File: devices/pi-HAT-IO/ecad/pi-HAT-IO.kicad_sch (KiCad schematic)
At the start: 49 parts, among them J1 GPIO, J10 JST XH, J2 Mini-Fit Jr, J3 JST SH, J4 JST SH, J5 JST SH, J6 PC FAN HEADER, J7 PC FAN HEADER, J8 JST PH, J9 JST PH, Q1 SI4477DY-T1-GE3, Q2 DMMT5401-7-F, Q3 DMG2305UX, Q4 DMG2305UX, U1 TLV75733PDBV, U2 PMU8418, U3 TCA9406DCTR, U4 EMC2302, U5 MCP9804_DFN

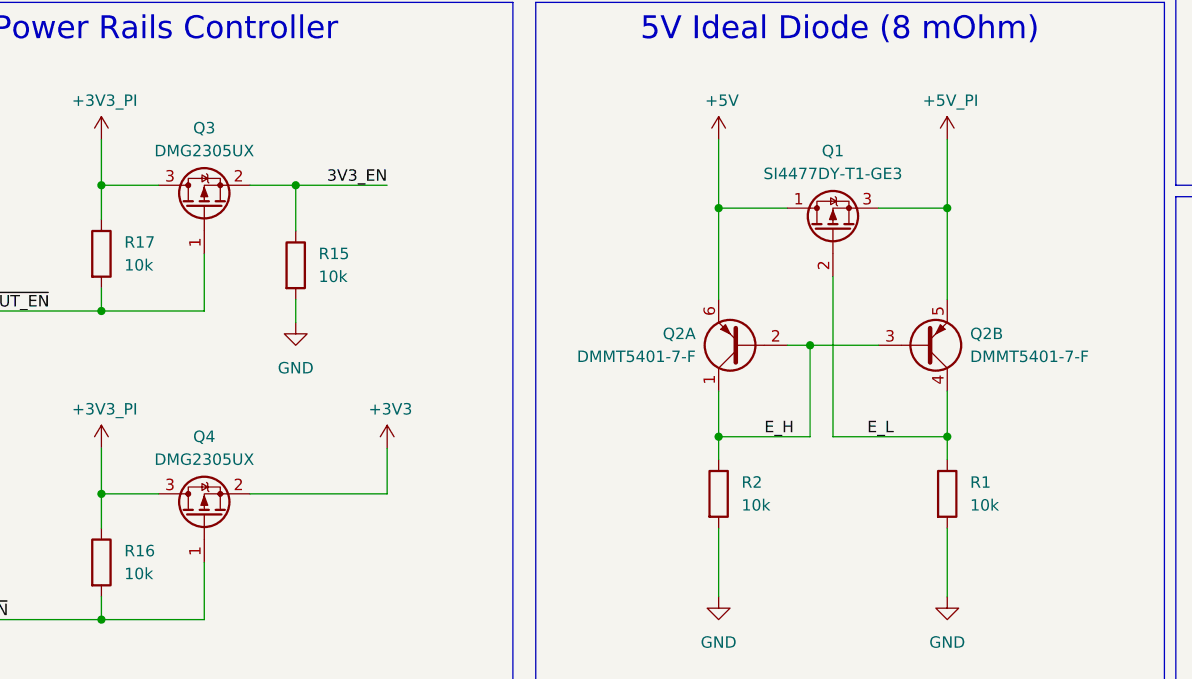
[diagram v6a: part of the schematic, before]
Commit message: Corrects PCB for production'
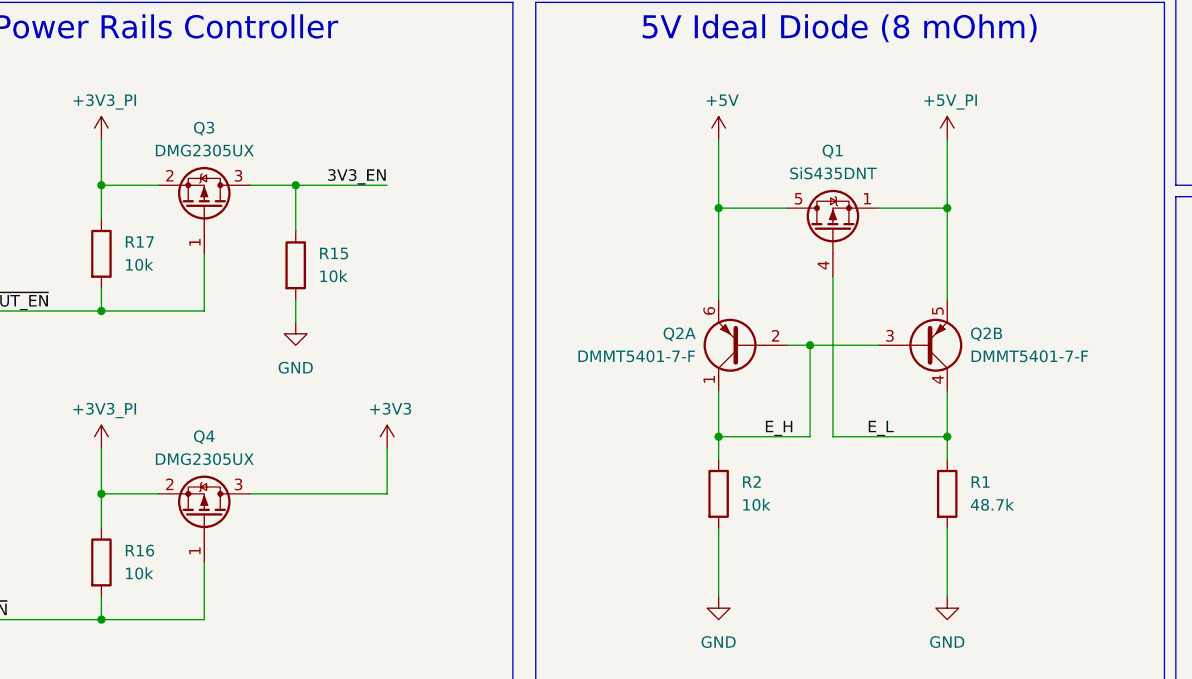
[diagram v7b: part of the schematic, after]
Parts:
- removed Q1: SI4477DY-T1-GE3, Package_SO:SO-8_3.9x4.9mm_P1.27mm, symbol Device:Q_PMOS_DGS
- added Q1: SiS435DNT, Package_SO:Vishay_PowerPAK_1212-8_Single, symbol Transistor_FET:SiS415DNT
- R1: value 10k -> 48.7k
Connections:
- net +3V3: now also Q4.3 (D); no longer Q4.2 (S)
- net +3V3_PI: now also Q3.2 (S), Q4.2 (S); no longer Q3.3 (D), Q4.3 (D)
- net +5V: now also Q1.5 (D)
- net +5V_PI: now also Q1.1 (S), Q1.2 (S), Q1.3 (S)
- net 3V3_EN: now also Q3.3 (D); no longer Q3.2 (S)
- net E_L: now also Q1.4 (G)
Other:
- moved on the sheet: Q3, Q4
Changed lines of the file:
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@@
 			)
 		)
-		(property "Value" "10k"
+		(property "Value" "48.7k"
 			(at 288.29 128.2699 0)
 			(effects
@@
 	)
 	(symbol
-		(lib_id "Device:Q_PMOS_DGS")
-		(at 273.05 97.79 90)
-		(unit 1)
-		(exclude_from_sim no)
-		(in_bom yes)
-		(on_board yes)
-		(dnp no)
-		(fields_autoplaced yes)
-		(property "Reference" "Q1"
-			(at 273.05 88.9 90)
-			(effects
-				(font
-					(size 1.27 1.27)
-				)
-			)
-		)
-		(property "Value" "SI4477DY-T1-GE3"
-			(at 273.05 91.44 90)
-			(effects
-				(font
-					(size 1.27 1.27)
-				)
-			)
-		)
-		(property "Footprint" "Package_SO:SO-8_3.9x4.9mm_P1.27mm"
-			(at 270.51 92.71 0)
-			(effects
-				(font
-					(size 1.27 1.27)
-				)
-				(hide yes)
-			)
-		)
-		(property "Datasheet" "~"
-			(at 273.05 97.79 0)
-			(effects
-				(font
-					(size 1.27 1.27)
-				)
-				(hide yes)
-			)
-		)
-		(property "Description" "P-MOSFET transistor, drain/gate/source"
-			(at 273.05 97.79 0)
-			(effects
-				(font
-					(size 1.27 1.27)
-				)
-				(hide yes)
-			)
-		)
-		(property "MPN" "SI4477DY-T1-GE3"
-			(at 273.05 97.79 90)
-			(effects
-				(font
-					(size 1.27 1.27)
-				)
-				(hide yes)
-			)
-		)
-		(property "Power Rating" ""
-			(at 273.05 97.79 0)
-			(effects
-				(font
-					(size 1.27 1.27)
-				)
-				(hide yes)
-			)
-		)
-		(property "Tolerance" ""
-			(at 273.05 97.79 0)
-			(effects
-				(font
-					(size 1.27 1.27)
-				)
-				(hide yes)
-			)
-		)
-		(property "Manufacturer" "Vishay Siliconix"
-			(at 273.05 97.79 0)
-			(effects
-				(font
-					(size 1.27 1.27)
-				)
-				(hide yes)
-			)
-		)
-		(pin "2"
-		)
-		(pin "3"
-		)
-		(pin "1"
-		)
-		(instances
-			(project "pi-HAT-IO"
-				(path "/e63e39d7-6ac0-4ffd-8aa3-1841a4541b55"
-					(reference "Q1")
-					(unit 1)
-				)
-			)
-		)
-	)
-	(symbol
 		(lib_id "power:+5V")
 		(at 346.71 26.67 0)
@@
 	)
 	(symbol
+		(lib_id "Transistor_FET:SiS415DNT")
+		(at 273.05 97.79 90)
+		(unit 1)
+		(exclude_from_sim no)
+		(in_bom yes)
+		(on_board yes)
+		(dnp no)
+		(fields_autoplaced yes)
+		(property "Reference" "Q1"
+			(at 273.05 88.9 90)
+			(effects
+				(font
+					(size 1.27 1.27)
+				)
+			)
+		)
+		(property "Value" "SiS435DNT"
+			(at 273.05 91.44 90)
+			(effects
+				(font
+					(size 1.27 1.27)
+				)
+			)
+		)
+		(property "Footprint" "Package_SO:Vishay_PowerPAK_1212-8_Single"
+			(at 274.955 92.71 0)
+			(effects
+				(font
+					(size 1.27 1.27)
+					(italic yes)
+				)
+				(justify left)
+				(hide yes)
+			)
+		)
+		(property "Datasheet" "https://www.vishay.com/docs/63684/sis435dnt.pdf"
+			(at 276.86 92.71 0)
+			(effects
+				(font
+					(size 1.27 1.27)
+				)
+				(justify left)
+				(hide yes)
+			)
+		)
+		(property "Description" "-30A Id, -20V Vds, P-Channel MOSFET, PowerPAK 1212-8 Single"
+			(at 273.05 97.79 0)
+			(effects
+				(font
+					(size 1.27 1.27)
+				)
+				(hide yes)
+			)
+		)
+		(pin "2"
+		)
+		(pin "4"
+		)
+		(pin "5"
+		)
+		(pin "1"
+		)
+		(pin "3"
+		)
+		(instances
+			(project "pi-HAT-IO"
+				(path "/e63e39d7-6ac0-4ffd-8aa3-1841a4541b55"
+					(reference "Q1")
+					(unit 1)
+				)
+			)
+		)
+	)
+	(symbol
 		(lib_id "power:GND")
 		(at 256.54 190.5 0)
@@
 	(symbol
 		(lib_id "Device:Q_PMOS_GSD")
-		(at 203.2 95.25 90)
+		(at 203.2 95.25 270)
+		(mirror x)
 		(unit 1)
 		(exclude_from_sim no)
@@
 		(on_board yes)
 		(dnp no)
-		(fields_autoplaced yes)
 		(property "Reference" "Q3"
 			(at 203.2 86.36 90)
@@
 		)
 		(property "Footprint" "Package_TO_SOT_SMD:SOT-23"
-			(at 200.66 90.17 0)
+			(at 205.74 90.17 0)
 			(effects
 				(font
@@
 	(symbol
 		(lib_id "Device:Q_PMOS_GSD")
-		(at 203.2 129.54 90)
+		(at 203.2 129.54 270)
+		(mirror x)
 		(unit 1)
 		(exclude_from_sim no)
@@
 		(on_board yes)
 		(dnp no)
-		(fields_autoplaced yes)
 		(property "Reference" "Q4"
 			(at 203.2 120.65 90)
@@
 		)
 		(property "Footprint" "Package_TO_SOT_SMD:SOT-23"
-			(at 200.66 124.46 0)
+			(at 205.74 124.46 0)
 			(effects
 				(font
